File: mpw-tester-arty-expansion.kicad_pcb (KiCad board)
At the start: 4 copper layers, 53.3 x 61.5 mm, 139 parts, among them J1 USB4105-GF-A, J10 61300211121, J11 61300211121, J12 61300211121, J14 61300311121, J15 61300311121, J18 61300411121, J19 61300711121, J20 61300411121, J3 Arty_A7_SPI, J4 61300211121, J5 61300311121, J6 61300211121, J7 61300211121, J8 61300211121, J9 61300211121, Q1 DTC014TEBTL, SW1 JS202011JCQN, SW2 JS202011JCQN, SW3 JS202011JCQN, U1 SN74LVC1G125DCKR, U10 TPD4E02B04DQA, U2 FT232HQ, U3 SN74LVC1G125DCKR, U4 MAX811REUS+T, U5 NTS0102DP, U6 MCP4661-103E/ML, U7 Caravel_breakout_PCB, U8 W25Q32FVSS, U9 MIC2211-AAYML-TR, Y1 ABM8G-12.000MHZ-18-D2Y-T, Y2 ECS-2520MVLC-100-BN-TR

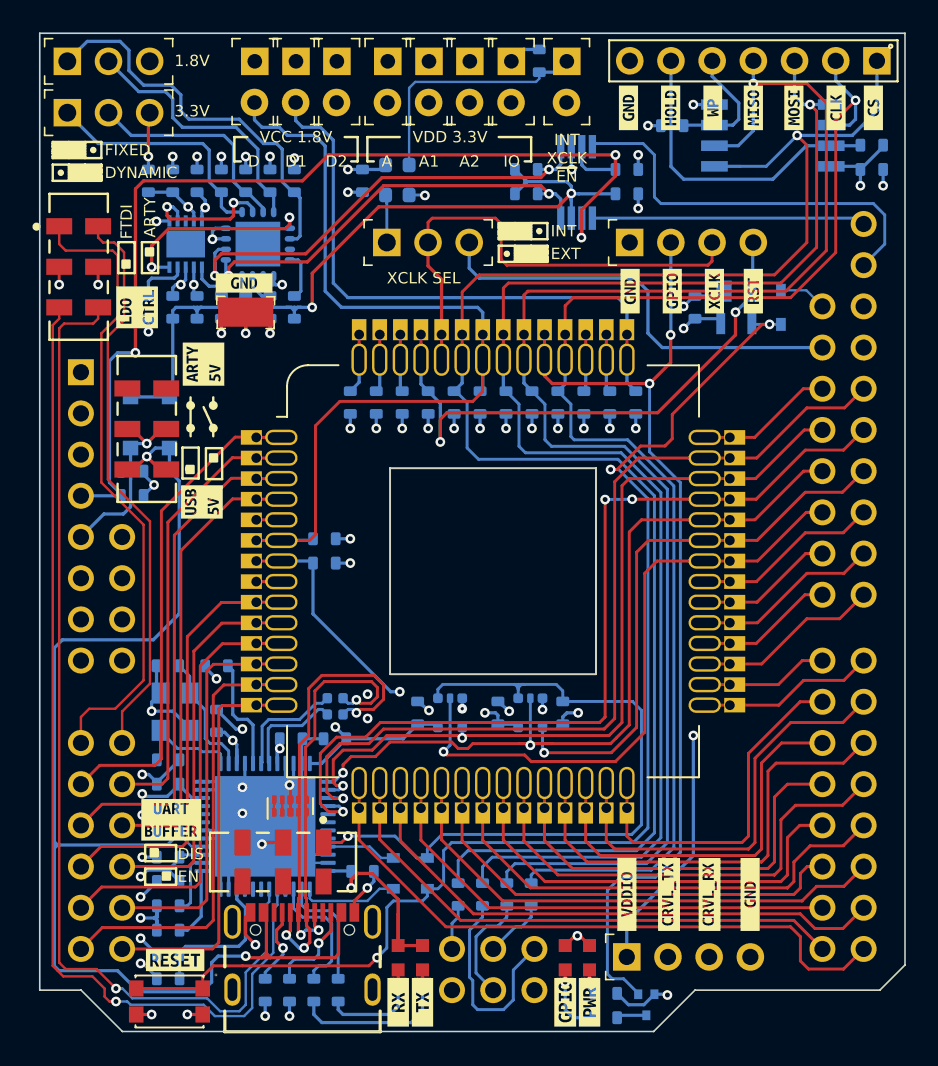
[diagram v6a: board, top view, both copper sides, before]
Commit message: Update footprints, add courtyard to Arty connectors, minor layout optimizations
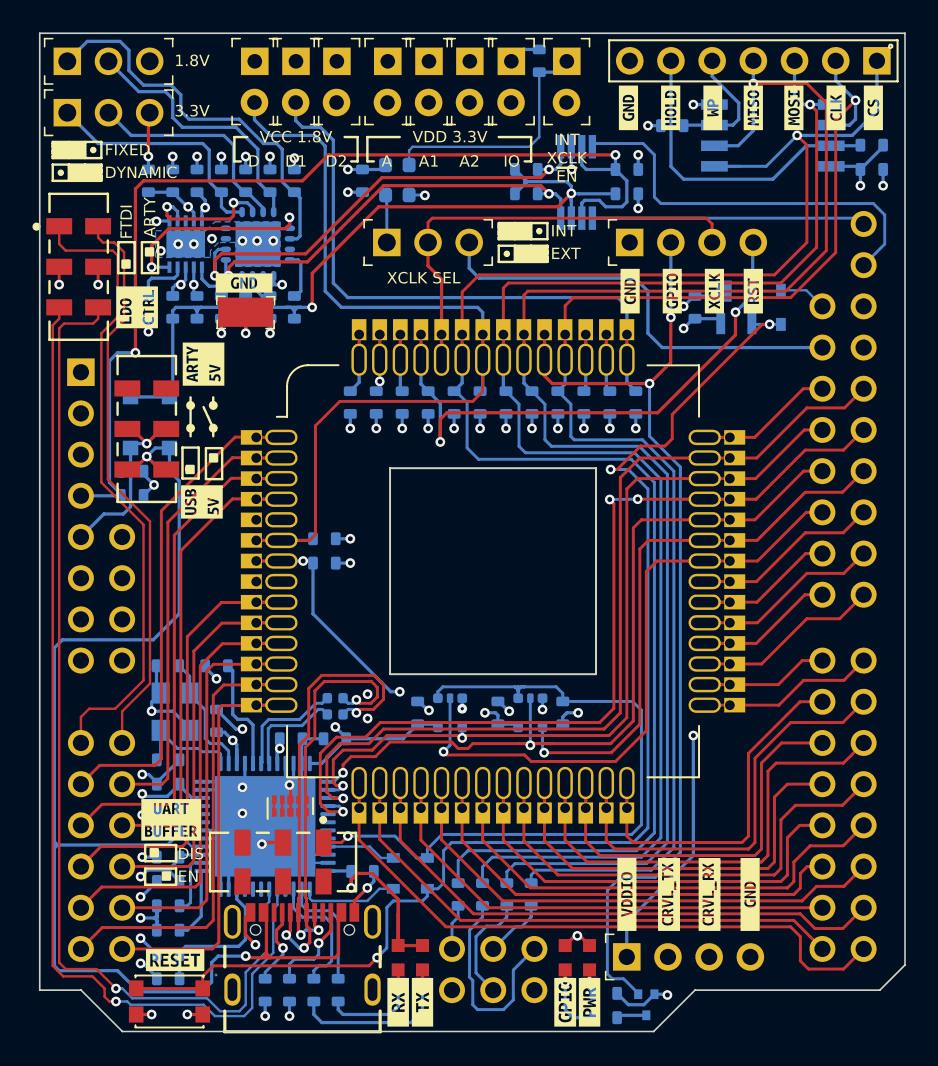
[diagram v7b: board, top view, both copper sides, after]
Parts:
- J3: value Arty_A7_SPI -> arty_chipKIT_connector
- moved R14 1.50 mm to (151.8, 119.1)
- moved R15 1.50 mm to (150.3, 119.1)
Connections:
- R14 pad 1: /ARTY_MEM_MOSI -> /ARTY_MEM_MISO
- R14 pad 2: /MEM.SI -> /MEM.SO
- R15 pad 1: /ARTY_MEM_MISO -> /ARTY_MEM_MOSI
- R15 pad 2: /MEM.SO -> /MEM.SI
- U6 pad 17: (no net) -> AGND
- U9 pad 11: (no net) -> AGND
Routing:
- net AGND: track 135.7 -> 130.4 mm, vias 55 -> 61
- net /VDDIO: track 84.9 -> 82.2 mm, vias 2 -> 4
- net /CRVL_XCLK: track 30.2 -> 27.7 mm
- net /3V3_ARTY: track 64.8 -> 64.0 mm, vias 3 -> 2
- net /MEM.SCK: track 82.2 -> 82.7 mm
- net /MEM.SO: track 92.4 -> 92.9 mm
- added copper zone on B.Cu, net AGND
